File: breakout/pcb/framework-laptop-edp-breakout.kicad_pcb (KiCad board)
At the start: 2 copper layers, 29 x 46 mm, 6 parts, among them J1 20879-040E-01, J2 Conn_01x40

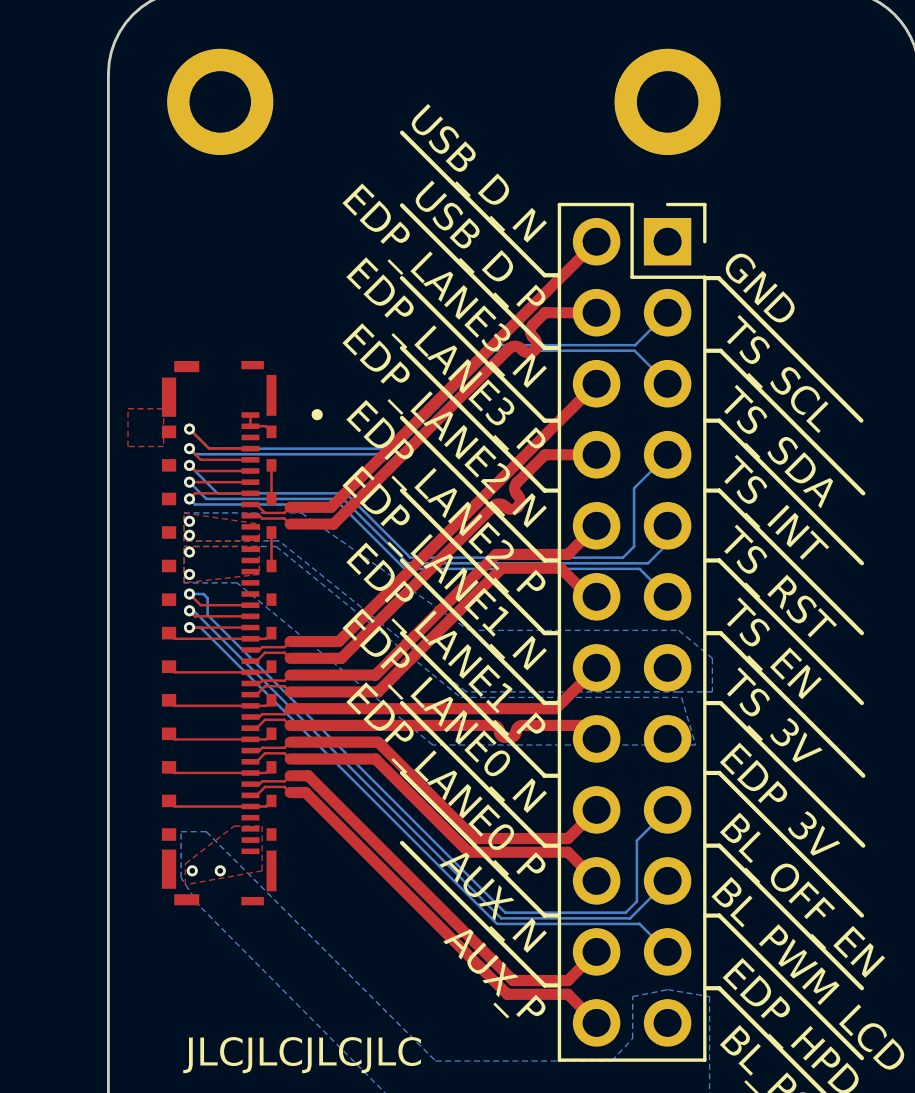
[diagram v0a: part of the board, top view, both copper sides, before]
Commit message: bigger vias on the breakout & remove some of em
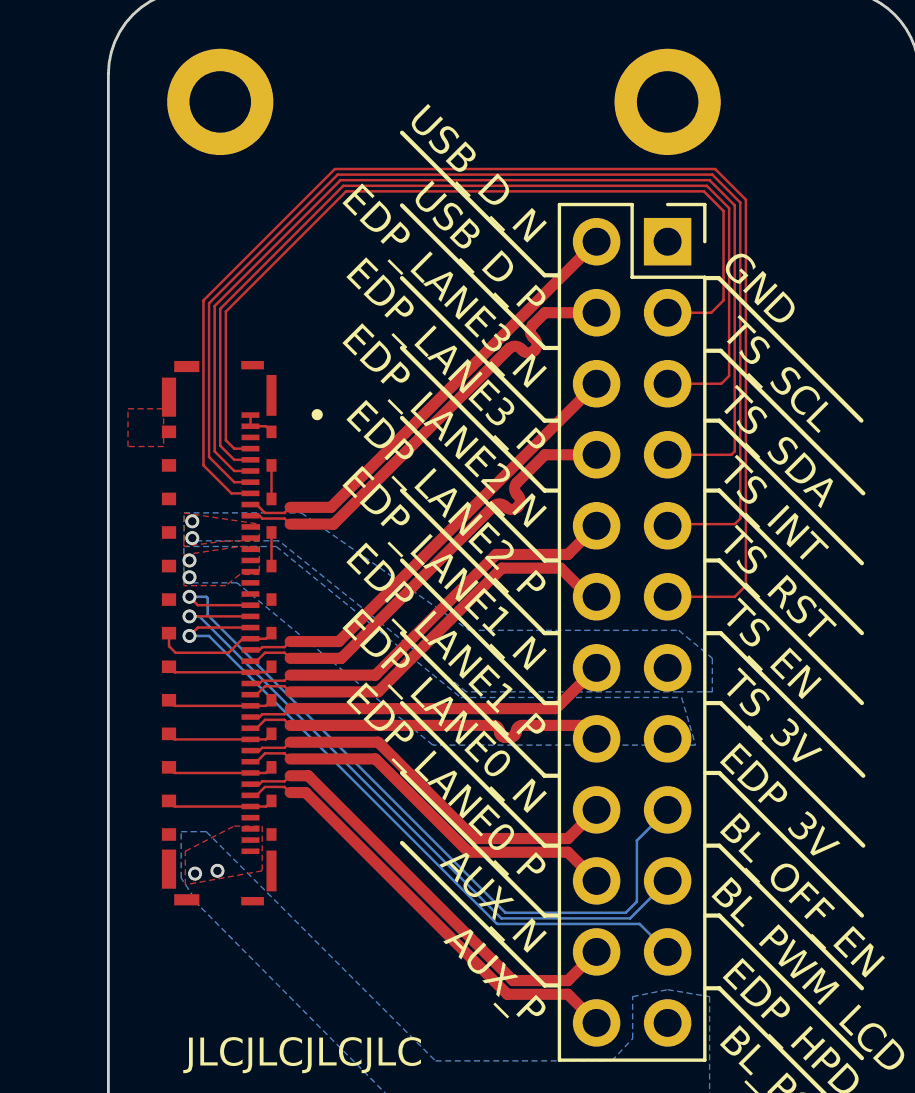
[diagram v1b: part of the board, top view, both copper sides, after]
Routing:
- net TS_EN: track 20.8 -> 46.6 mm, vias 1 -> 0
- net TS_RST: track 21.4 -> 42.7 mm, vias 1 -> 0
- net TS_INT_N: track 23.5 -> 38.9 mm, vias 1 -> 0
- net TS_SDA: track 21.6 -> 34.9 mm, vias 1 -> 0
- net TS_SCL: track 21.9 -> 30.9 mm, vias 1 -> 0
- net GND: track 26.6 -> 27.3 mm

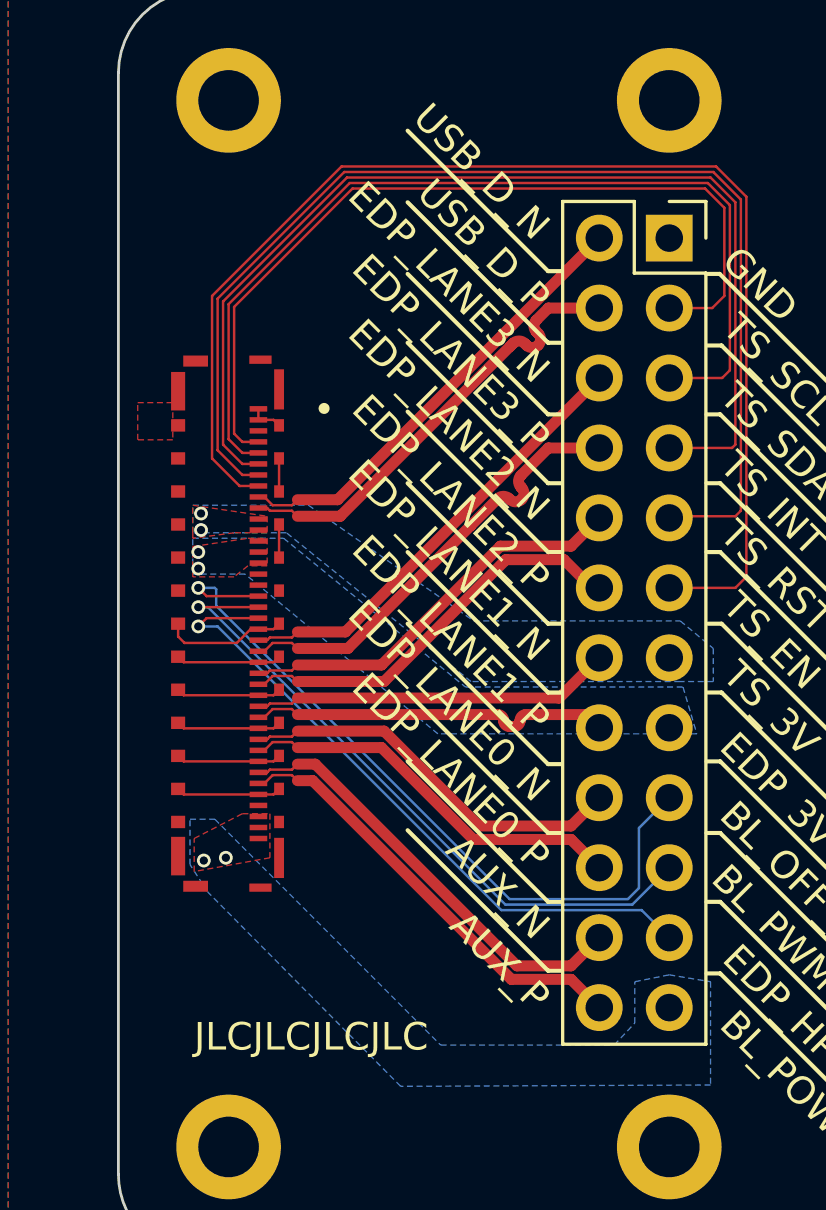
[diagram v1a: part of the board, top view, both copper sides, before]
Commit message: improve power rails on the breakout
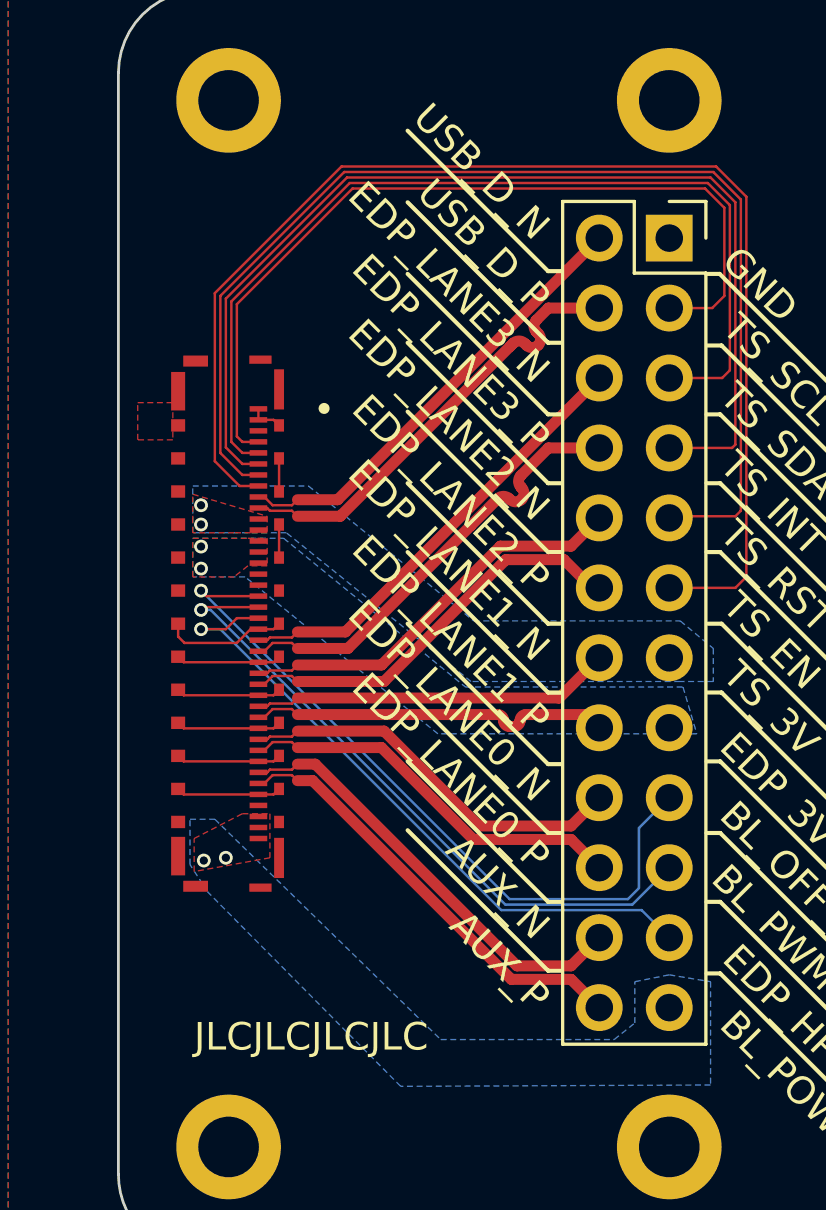
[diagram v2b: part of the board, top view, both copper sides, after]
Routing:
- net BL_OFF_EN: track 27.2 -> 26.6 mm
